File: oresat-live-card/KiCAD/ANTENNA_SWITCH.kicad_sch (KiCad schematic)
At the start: 0 parts

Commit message: added RF scwitches
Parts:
- added C100, C102, C96: 100p, symbol Device:C_Small
- added C101: 100n, symbol Device:C_Small
- added C94, C95: 100n, Resistor_SMD:R_0603_1608Metric, symbol Device:C_Small
- added J13: 2X1_TH_JUMPER, oresat-live-card:2X1, symbol Jumper:Jumper_2_Open
- added R110, R112: 10k, symbol Device:R_US
- added R111, R113: 5.62k, symbol Device:R_US
- added U30: SN74LV1T34DCK, Package_TO_SOT_SMD:SOT-353_SC-70-5, symbol Logic_LevelTranslator:SN74LV1T34DCK
- added U31: SN74LVC1G32QDBVRQ1, oresat-live-card:DBV5, symbol oresat-ics:SN74LVC1G32QDBVRQ1
- added U33: QPC1022, oresat-ics:QPC1022, symbol oresat-ics:QPC1022
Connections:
- new net: C102.1, R112.1, R113.2, U33.6 (EN)
- new net: U30.4 (Y), U31.2 (B)
- new net: J13.2 (B), U31.1 (A)
- new net: R110.1, U31.4 (Y)
- new net: C96.1, R110.2, R111.2, U33.5 (CTRL)
- new net 5V: C100.1, C101.1, C94.1, C95.1, J13.1 (A), R112.2, U30.5 (VCC), U31.5 (VCC), U33.7 (VDD)
- new net ANT_SEL: U30.2 (A)
- new net GND: C100.2, C101.2, C102.2, C94.2, C95.2, C96.2, R111.1, R113.1, U30.3 (GND), U31.3 (GND), U33.1 (GND), U33.3 (GND), U33.9 (GND)
- new net HELIX_ANTENNA: U33.4 (RF1)
- new net TURNSTILE_ANTENNA: U33.8 (RF2)
- new net TX_RX_COMMON: U33.2 (RF_COM)

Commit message: implemented notes from Oliver. Added notes for self to fix later
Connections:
- net HELIX_ANTENNA: now also U33.8 (RF2); no longer U33.4 (RF1)
- net TURNSTILE_ANTENNA: now also U33.4 (RF1); no longer U33.8 (RF2)
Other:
- note added: "1K SERIES?"
- note added: "3.3V TO 5.0V LEVEL TRANSLATE"
- note added: "ADD 10K PULL DOWN"
- note added: "CTRL OUTPUT HIGH TURNSTILE ANTENNA(RF1) LOW HELIX ANTENNA (RF2)"
- note added: "INSTALL JUMPER TO SELECT TURNSTILE ANTENNA"
- note added: "MAKE LOOK BETTER"
- note added: "VERIFY LOGIC MATCHES TABLE AND DEFAULTS TO HELIX"
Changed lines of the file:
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@@
 	(paper "B")
 	(title_block
+		(date "2025-05-28")
 		(rev "2")
+	)
+	(text "INSTALL JUMPER TO SELECT TURNSTILE ANTENNA\n"
+		(exclude_from_sim no)
+		(at 112.268 80.772 0)
+		(effects
+			(font
+				(size 1.27 1.27)
+			)
+		)
+	)
+	(text "CTRL    OUTPUT\nHIGH    TURNSTILE ANTENNA(RF1)\nLOW     HELIX ANTENNA (RF2)"
+		(exclude_from_sim no)
+		(at 280.416 226.06 0)
+		(effects
+			(font
+				(size 1.27 1.27)
+			)
+			(justify left)
+		)
+	)
+	(text "VERIFY LOGIC MATCHES TABLE AND DEFAULTS TO HELIX"
+		(exclude_from_sim no)
+		(at 288.544 207.518 0)
+		(effects
+			(font
+				(size 1.27 1.27)
+			)
+		)
+	)
+	(text "ADD 10K PULL DOWN"
+		(exclude_from_sim no)
+		(at 149.606 77.724 0)
+		(effects
+			(font
+				(size 1.27 1.27)
+			)
+		)
+	)
+	(text "MAKE LOOK BETTER\n"
+		(exclude_from_sim no)
+		(at 289.56 220.218 0)
+		(effects
+			(font
+				(size 1.27 1.27)
+			)
+		)
+	)
+	(text "3.3V TO 5.0V LEVEL TRANSLATE"
+		(exclude_from_sim no)
+		(at 89.154 113.284 0)
+		(effects
+			(font
+				(size 1.27 1.27)
+			)
+		)
+	)
+	(text "1K SERIES?"
+		(exclude_from_sim no)
+		(at 111.506 70.866 0)
+		(effects
+			(font
+				(size 1.27 1.27)
+			)
+		)
 	)
 	(junction
@@
 		)
 	)
-	(global_label "TURNSTILE_ANTENNA"
+	(global_label "HELIX_ANTENNA"
 		(shape input)
 		(at 297.18 210.82 0)
@@
 		)
 		(property "Intersheetrefs" "${INTERSHEET_REFS}"
-			(at 319.2757 210.82 0)
+			(at 314.74 210.82 0)
+			(effects
+				(font
+					(size 0.889 0.889)
+				)
+				(justify left)
+			)
+		)
+	)
+	(global_label "TURNSTILE_ANTENNA"
+		(shape input)
+		(at 297.18 200.66 0)
+		(fields_autoplaced yes)
+		(effects
+			(font
+				(size 1.27 1.27)
+			)
+			(justify left)
+		)
+		(property "Intersheetrefs" "${INTERSHEET_REFS}"
+			(at 319.2757 200.66 0)
 			(effects
 				(font
@@
 			)
 		)
-	)
-	(global_label "HELIX_ANTENNA"
-		(shape input)
-		(at 297.18 200.66 0)
-		(fields_autoplaced yes)
-		(effects
-			(font
-				(size 1.27 1.27)
-			)
-			(justify left)
-		)
-		(property "Intersheetrefs" "${INTERSHEET_REFS}"
-			(at 314.74 200.66 0)
-			(effects
-				(font
-					(size 0.889 0.889)
-				)
-				(justify left)
-			)
-		)

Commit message: implemented notes form Oliver J
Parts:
- added R101: 1K, symbol Device:R_US
- added R102: 10K, symbol Device:R_US
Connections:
- net 5V: now also R101.1; no longer J13.1 (A)
- net GND: now also R102.2
- net at J13.2 (B), U31.1 (A): now also R102.1
- new net: J13.1 (A), R101.2
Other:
- note removed: "1K SERIES?"
- note removed: "ADD 10K PULL DOWN"
- note removed: "CTRL OUTPUT HIGH TURNSTILE ANTENNA(RF1) LOW HELIX ANTENNA (RF2)"
- note removed: "MAKE LOOK BETTER"

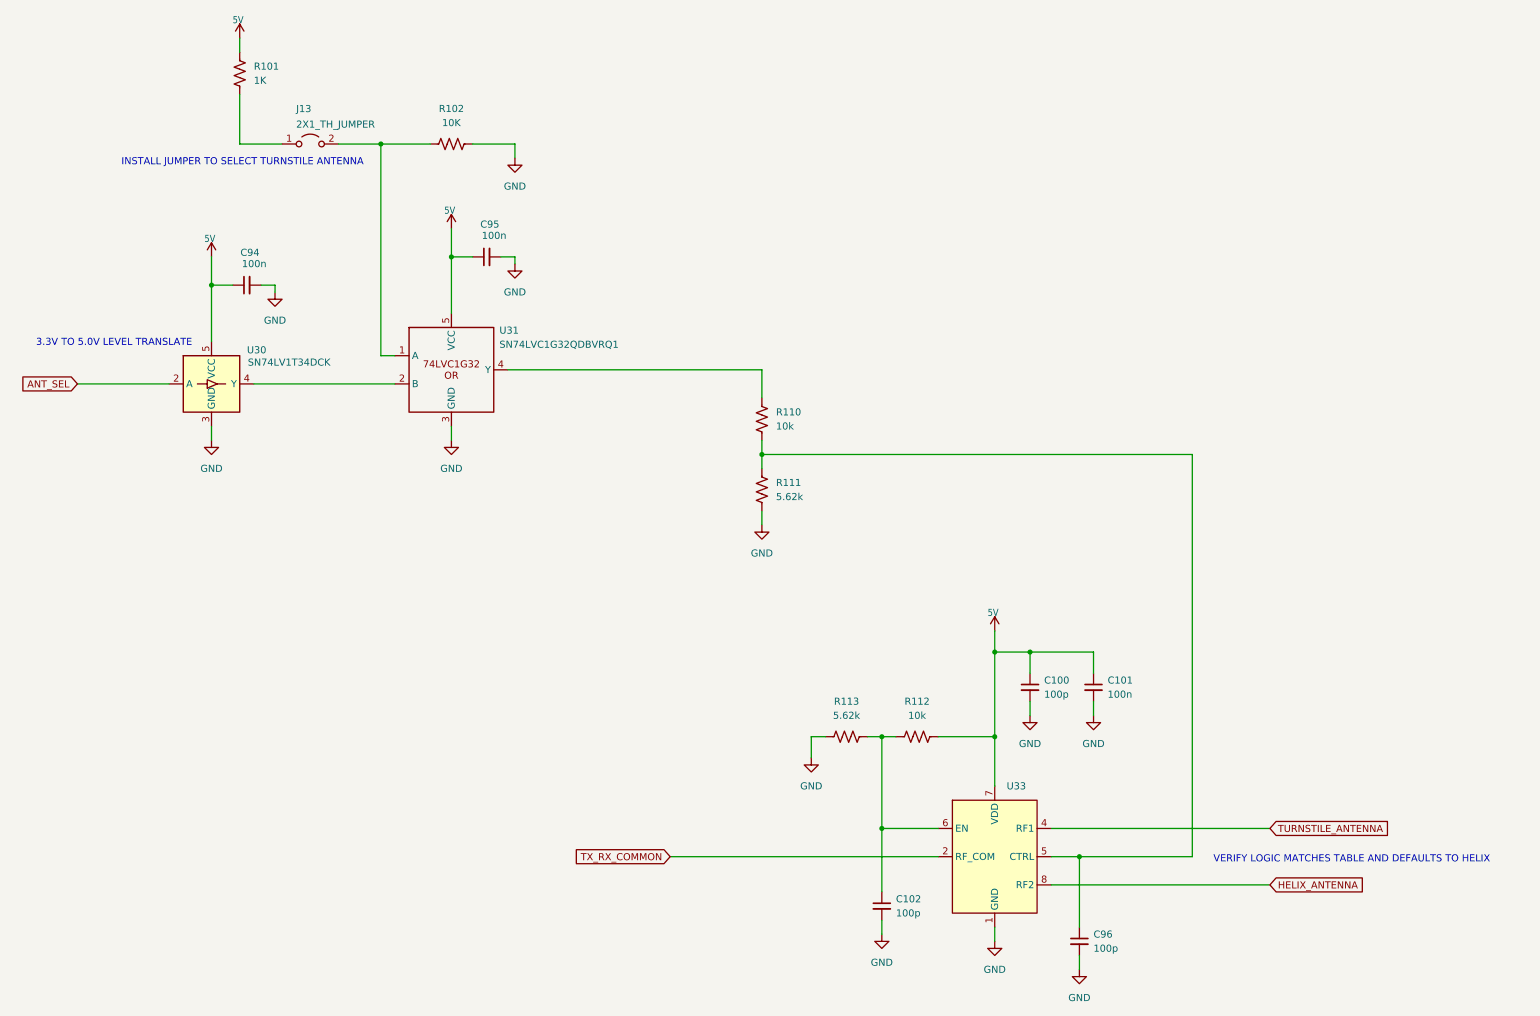
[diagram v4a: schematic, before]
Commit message: Fixed up schematic as best as possible. There were a lot of issues with local paths being referenced, and EAGLE import libraries. Fixed all of those, as well as fixed some oresat-kicad IC symbols (bad direction pins) and I think we're now OK. Also updated card outline for two RF (LEFT) connectors.  Still missing two packages, but we'll deal with that later.
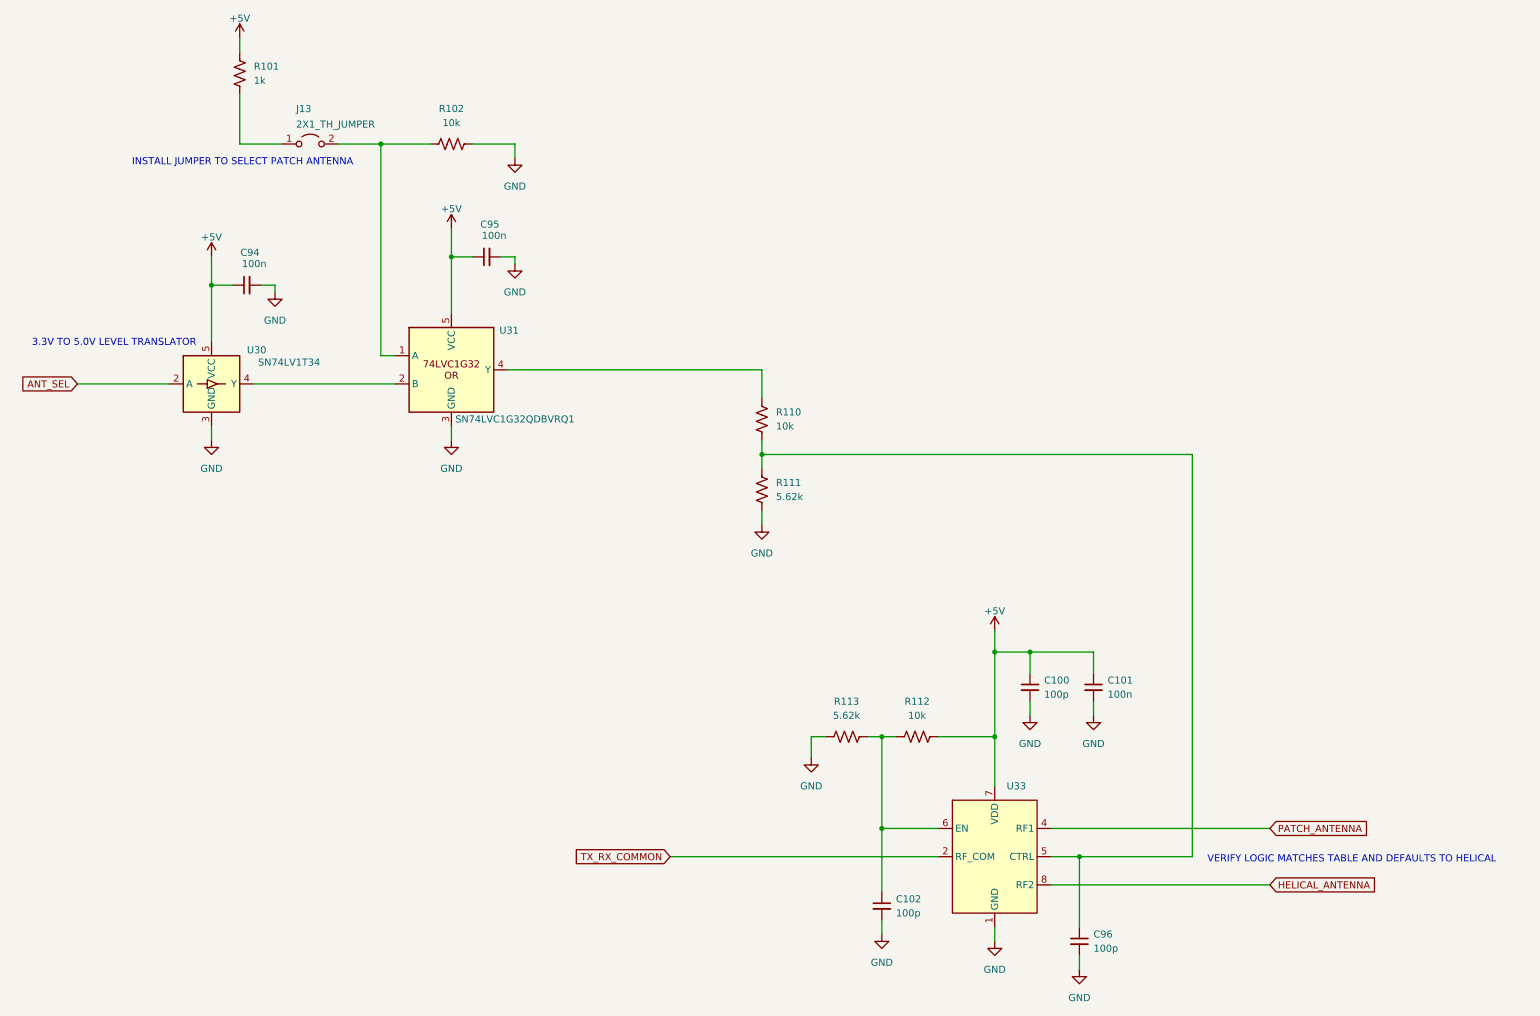
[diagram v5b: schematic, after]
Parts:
- C100, C102: footprint (none) -> Resistor_SMD:R_0402_1005Metric; DPN (none) -> 490-GCM1555C1H101GA16DCT-ND; Distributor (none) -> DigiKey; MFR (none) -> Murata Electronics; MPN (none) -> GCM1555C1H101GA16D
- C101: footprint (none) -> Resistor_SMD:R_0603_1608Metric; DPN (none) -> 445-5667-1-ND; Distributor (none) -> DigiKey; MFR (none) -> TDK Corporation; MPN (none) -> CGA3E2X7R1E104K080AA
- C94, C95: DPN (none) -> 445-5667-1-ND; MFR (none) -> TDK Corporation; MPN CL10B104KB8WPNC -> CGA3E2X7R1E104K080AA
- C96: footprint (none) -> Resistor_SMD:R_0402_1005Metric; DPN (none) -> 490-GCM1555C1H101GA16DCT-ND; Distributor (none) -> DigiKey; MFR (none) -> Murata Electronics; MPN GCM1555C1H101JA16D -> GCM1555C1H101GA16D
- R101: value 1K -> 1k; footprint (none) -> Resistor_SMD:R_0603_1608Metric; DPN (none) -> P1.00KHCT-ND; Distributor (none) -> DigiKey; MFR (none) -> Panasonic; MPN (none) -> ERJ-3EKF1001V
- R102: value 10K -> 10k; footprint (none) -> Resistor_SMD:R_0603_1608Metric; DPN (none) -> P10.0KHCT-ND; Distributor (none) -> DigiKey; MFR (none) -> Panasonic; MPN (none) -> ERJ-3EKF1002V
- R110, R112: footprint (none) -> Resistor_SMD:R_0603_1608Metric; DPN (none) -> P10.0KHCT-ND; Distributor (none) -> DigiKey; MFR (none) -> Panasonic; MPN (none) -> ERJ-3EKF1002V
- R111, R113: footprint (none) -> Resistor_SMD:R_0603_1608Metric; DPN (none) -> P5.62KHCT-ND; Distributor (none) -> DigiKey; MFR (none) -> Panasonic; MPN (none) -> ERJ-3EKF5621V
- U30: value SN74LV1T34DCK -> SN74LV1T34; DPN (none) -> 296-SN74LV1T34QDCKRQ1CT-ND; Distributor (none) -> DigiKey; MFR (none) -> Texas Instruments; MPN (none) -> SN74LV1T34QDCKRQ1
- U31: footprint oresat-live-card:DBV5 -> (none); Distributor DigiKey -> (none); MPN SN74LVC1G32QDBVRQ1 -> (none)
- U33: DPN (none) -> 2312-QPC1022TR7CT-ND; Distributor (none) -> DigiKey; MFR (none) -> Qorvo; MPN (none) -> QPC1022TR7
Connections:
- net 5V renamed +5V
- net HELIX_ANTENNA renamed HELICAL_ANTENNA
- net TURNSTILE_ANTENNA renamed PATCH_ANTENNA
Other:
- note added: "3.3V TO 5.0V LEVEL TRANSLATOR"
- note added: "INSTALL JUMPER TO SELECT PATCH ANTENNA"
- note added: "VERIFY LOGIC MATCHES TABLE AND DEFAULTS TO HELICAL"
- note removed: "3.3V TO 5.0V LEVEL TRANSLATE"
- note removed: "INSTALL JUMPER TO SELECT TURNSTILE ANTENNA"
- note removed: "VERIFY LOGIC MATCHES TABLE AND DEFAULTS TO HELIX"
